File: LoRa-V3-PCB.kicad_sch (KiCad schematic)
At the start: 85 parts, among them IC1 114993121, IC10 BR24G1MFVT-5AE2, IC11 BR24G1MFVT-5AE2, IC12 AEM00920, IC13 MCP73123T-22SI/MF, IC2 CP2102N-Axx-xQFN24, IC3 USBLC6-2P6, IC5 BME680, IC6 SHT40-BD1B-R2, IC7 TSL25911FN, IC8 BR24G1MFVT-5AE2, IC9 BR24G1MFVT-5AE2, Q1 PJC7400_R1_00001, Q2 Si2367DS, Q3 Si2367DS, Q4 Si2367DS, SW1 434331045822, SW2 SLLB510100

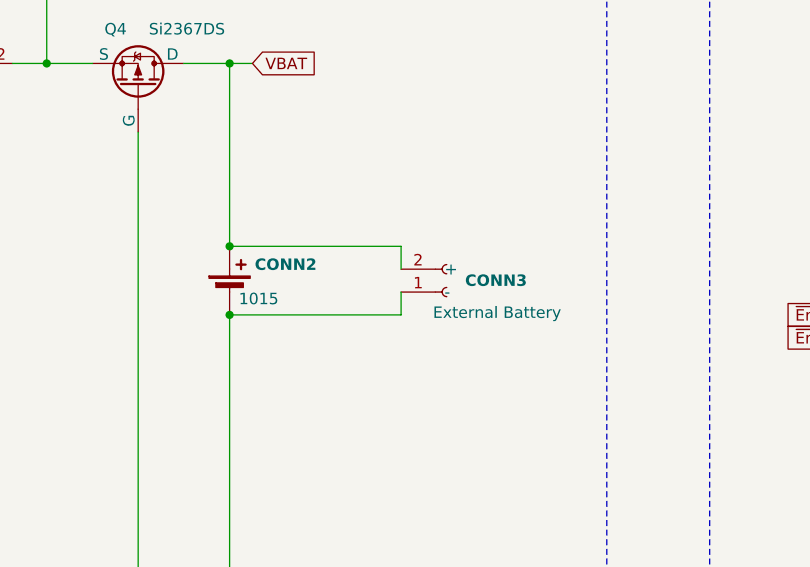
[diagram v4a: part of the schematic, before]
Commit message: fix footprints
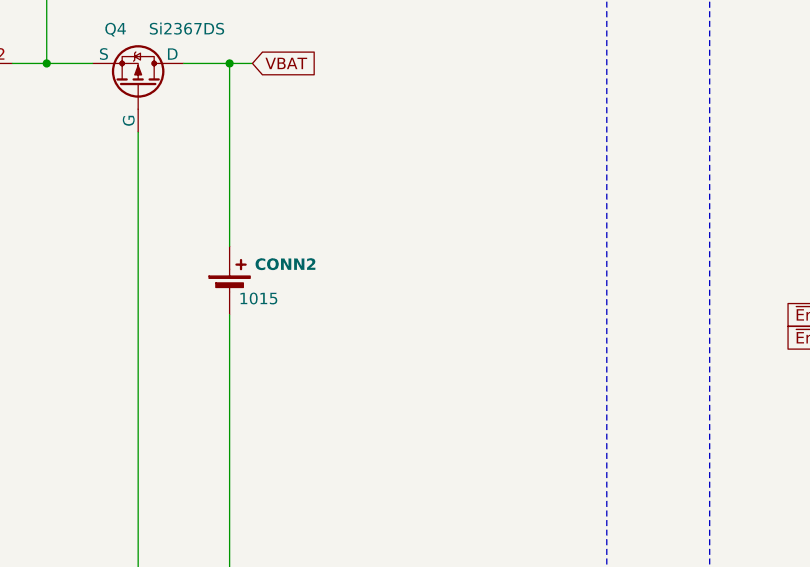
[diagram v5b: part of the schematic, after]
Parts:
- removed CONN3: B2B-XH-A(LF)(SN), 1projectLibrary:JST_XH_B2B-XH-A_1x02_P2.50mm_Vertical, symbol 1projectLibrary:Connector_2p_Battery
- H1, H2: footprint 1projectLibrary:MountingHole_2mm -> 1projectLibrary:MountingHole_2mm_noCourtyard
- IC10, IC11, IC8, IC9: footprint thisProjectLibrary:TSSOP-B8 -> 1projectLibrary:BR24G1M-TSSOP-B8
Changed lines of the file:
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@@
 	)
 	(junction
-		(at 250.19 101.6)
-		(diameter 0)
-		(color 0 0 0 0)
-	)
-	(junction
 		(at 97.79 345.44)
 		(diameter 0)
@@
 	)
 	(junction
-		(at 250.19 93.98)
-		(diameter 0)
-		(color 0 0 0 0)
-	)
-	(junction
 		(at 68.58 347.98)
 		(diameter 0)
@@
 	(wire
 		(pts
-			(xy 269.24 96.52) (xy 269.24 93.98)
-		)
-		(stroke
-			(width 0)
-			(type default)
-		)
-	)
-	(wire
-		(pts
 			(xy 116.84 384.81) (xy 92.71 384.81)
 		)
@@
 	(wire
 		(pts
-			(xy 269.24 93.98) (xy 250.19 93.98)
-		)
-		(stroke
-			(width 0)
-			(type default)
-		)
-	)
-	(wire
-		(pts
 			(xy 294.64 345.44) (xy 347.98 345.44)
 		)
@@
 	(wire
 		(pts
-			(xy 269.24 99.06) (xy 269.24 101.6)
-		)
-		(stroke
-			(width 0)
-			(type default)
-		)
-	)
-	(wire
-		(pts
 			(xy 144.78 83.82) (xy 144.78 81.28)
 		)
@@
 	(wire
 		(pts
-			(xy 269.24 101.6) (xy 250.19 101.6)
-		)
-		(stroke
-			(width 0)
-			(type default)
-		)
-	)
-	(wire
-		(pts
 			(xy 52.07 367.03) (xy 46.99 367.03)
 		)
@@
 			)
 		)
-		(property "Footprint" "thisProjectLibrary:TSSOP-B8"
+		(property "Footprint" "1projectLibrary:BR24G1M-TSSOP-B8"
 			(at 232.41 394.97 0)
 			(effects
@@
 	)
 	(symbol
-		(lib_id "1projectLibrary:Connector_2p_Battery")
-		(at 274.32 99.06 0)
-		(mirror x)
-		(unit 1)
-		(exclude_from_sim no)
-		(in_bom yes)
-		(on_board yes)
-		(dnp no)
-		(property "Reference" "CONN3"
-			(at 276.352 97.79 0)
-			(effects
-				(font
-					(size 1.27 1.27)
-					(bold yes)
-				)
-				(justify left)
-			)
-		)
-		(property "Value" "B2B-XH-A(LF)(SN)"
-			(at 273.05 92.71 0)
-			(effects
-				(font
-					(size 1.27 1.27)
-				)
-				(justify left)
-				(hide yes)
-			)
-		)
-		(property "Footprint" "1projectLibrary:JST_XH_B2B-XH-A_1x02_P2.50mm_Vertical"
-			(at 274.32 91.44 0)
-			(effects
-				(font
-					(size 1.27 1.27)
-				)
-				(hide yes)
-			)
-		)
-		(property "Datasheet" "https://www.farnell.com/datasheets/2057209.pdf"
-			(at 274.32 86.36 0)
-			(effects
-				(font
-					(size 1.27 1.27)
-				)
-				(hide yes)
-			)
-		)
-		(property "Description" "External Battery"
-			(at 279.908 101.346 0)
-			(effects
-				(font
-					(size 1.27 1.27)
-				)
-			)
-		)
-		(property "manufacturerName" "JST"
-			(at 274.32 82.55 0)
-			(effects
-				(font
-					(size 1.27 1.27)
-				)
-				(hide yes)
-			)
-		)
-		(property "octopartUrl" "https://octopart.com/b2b-xh-a%28lf%29%28sn%29-jst-7424860?r=sp"
-			(at 274.32 99.06 0)
-			(effects
-				(font
-					(size 1.27 1.27)
-				)
-				(hide yes)
-			)
-		)
-		(property "manufacturerPartNumber" "B2B-XH-A(LF)(SN)"
-			(at 274.32 99.06 0)
-			(effects
-				(font
-					(size 1.27 1.27)
-				)
-				(hide yes)
-			)
-		)
-		(pin "1"
-		)
-		(pin "2"
-		)
-		(instances
-			(project "LoRa-V3-PCB"
-				(path "/8b98a678-96e2-411a-8566-924f77e9f267"
-					(reference "CONN3")
-					(unit 1)
-				)
-			)
-		)
-	)
-	(symbol
 		(lib_id "Connector:Conn_01x06_Pin")
 		(at 370.84 31.75 270)
@@
 			)
 		)
-		(property "Footprint" "1projectLibrary:MountingHole_2mm"
+		(property "Footprint" "1projectLibrary:MountingHole_2mm_noCourtyard"
 			(at 518.16 332.74 0)
 			(effects
@@
 			)
 		)
-		(property "Footprint" "thisProjectLibrary:TSSOP-B8"
+		(property "Footprint" "1projectLibrary:BR24G1M-TSSOP-B8"
 			(at 265.43 394.97 0)
 			(effects
@@
 			)
 		)
-		(property "Footprint" "1projectLibrary:MountingHole_2mm"
+		(property "Footprint" "1projectLibrary:MountingHole_2mm_noCourtyard"
 			(at 518.16 337.82 0)
 			(effects
@@
 			)
 		)
-		(property "Footprint" "thisProjectLibrary:TSSOP-B8"
+		(property "Footprint" "1projectLibrary:BR24G1M-TSSOP-B8"
 			(at 299.72 394.97 0)
 			(effects
@@
 			)
 		)
-		(property "Footprint" "thisProjectLibrary:TSSOP-B8"
+		(property "Footprint" "1projectLibrary:BR24G1M-TSSOP-B8"
 			(at 198.12 394.97 0)
 			(effects

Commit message: several fixes
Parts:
- SW1: footprint 1GlobalFootprintsLibrary:Wurth-4343X10458XX -> 1projectLibrary:Wurth-4343X10458XX
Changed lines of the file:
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@@
 			)
 		)
-		(property "Footprint" "1GlobalFootprintsLibrary:Wurth-4343X10458XX"
+		(property "Footprint" "1projectLibrary:Wurth-4343X10458XX"
 			(at 388.112 152.654 0)
 			(effects

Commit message: fix SHT40 footprint
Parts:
- IC6: footprint 1GlobalFootprintsLibrary:SHT4X -> 1projectLibrary:SHT4X
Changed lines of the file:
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@@
 			)
 		)
-		(property "Footprint" "1GlobalFootprintsLibrary:SHT4X"
+		(property "Footprint" "1projectLibrary:SHT4X"
 			(at 71.12 402.59 0)
 			(effects

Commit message: wip
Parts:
- C24: value C0603C106M8PACTU -> 47uF 10V; footprint 1projectLibrary:C_0603_nominal -> Capacitor_Tantalum_SMD:CP_EIA-3528-12_Kemet-T; symbol Device:C -> Device:C_Polarized_Small; genericPartNumber GPC0603475-10-X7S -> (none); manufacturerName KEMET -> (none); manufacturerPartNumber C0603C106M8PACTU -> 293D476X9010B2TE3; octopartUrl https://octopart.com/c0603c106m8pactu-kemet-89187410?r=sp -> (none)
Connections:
- net GND: now also IC12.9 (SHIP_MODE)
- no-connect marks 31 -> 30
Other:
- moved on the sheet: Q2, R17, SW2
